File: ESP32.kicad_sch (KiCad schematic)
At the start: 39 parts, among them J4 JTAG, Q1 MMBT3904, Q2 MMBT3904, Q3 MMBT3904, Q4 MMBT3904, U1 ESP-WROVER-32, U3 CH340G, Y1 12M

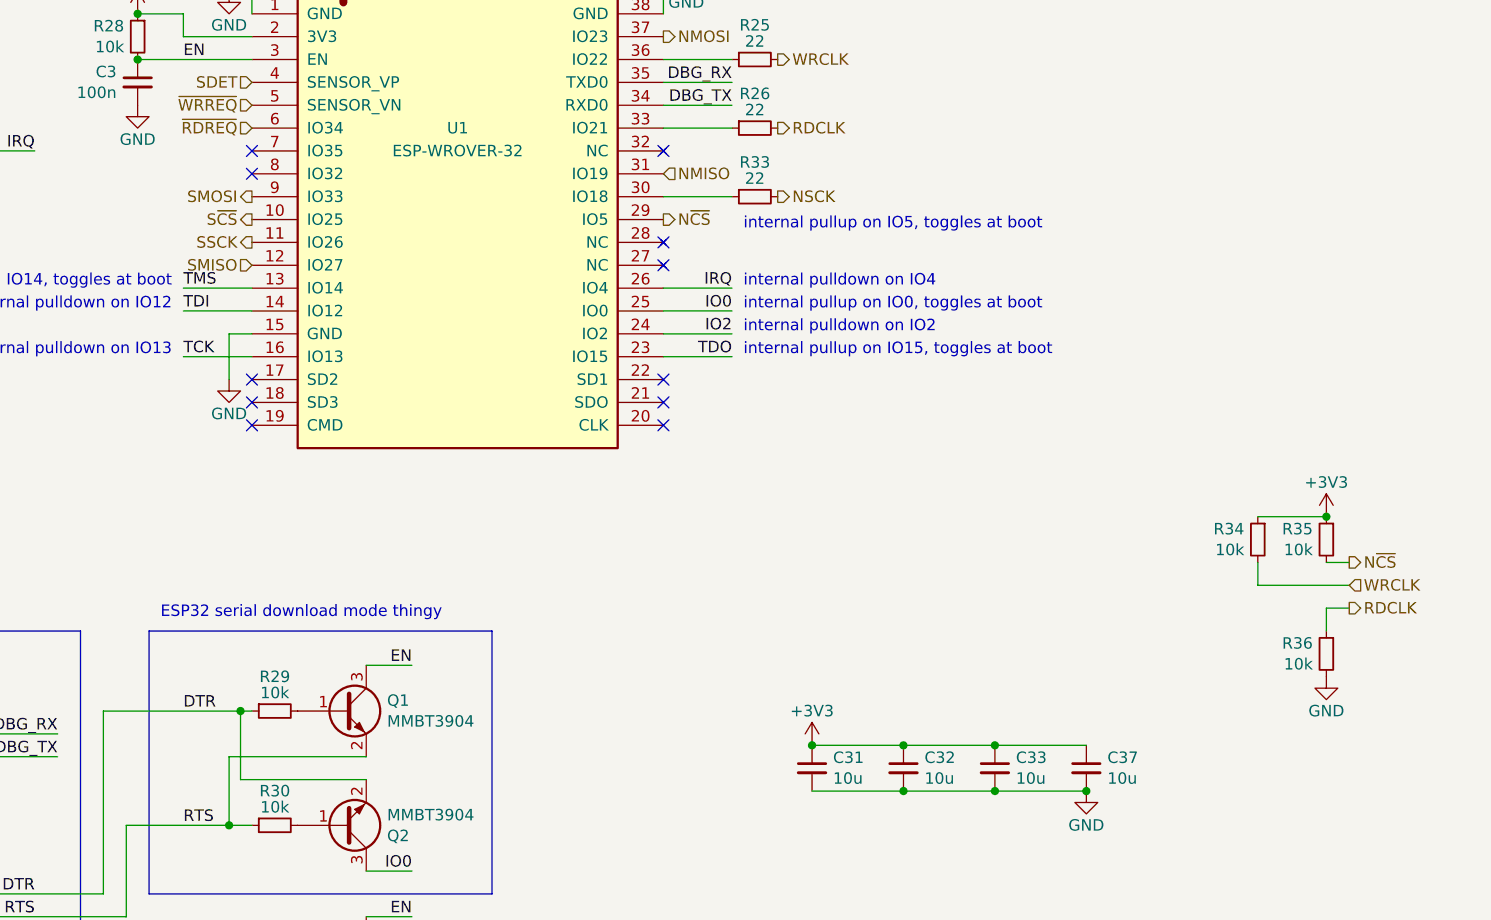
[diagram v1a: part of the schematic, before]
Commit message: Prototype with 74xx
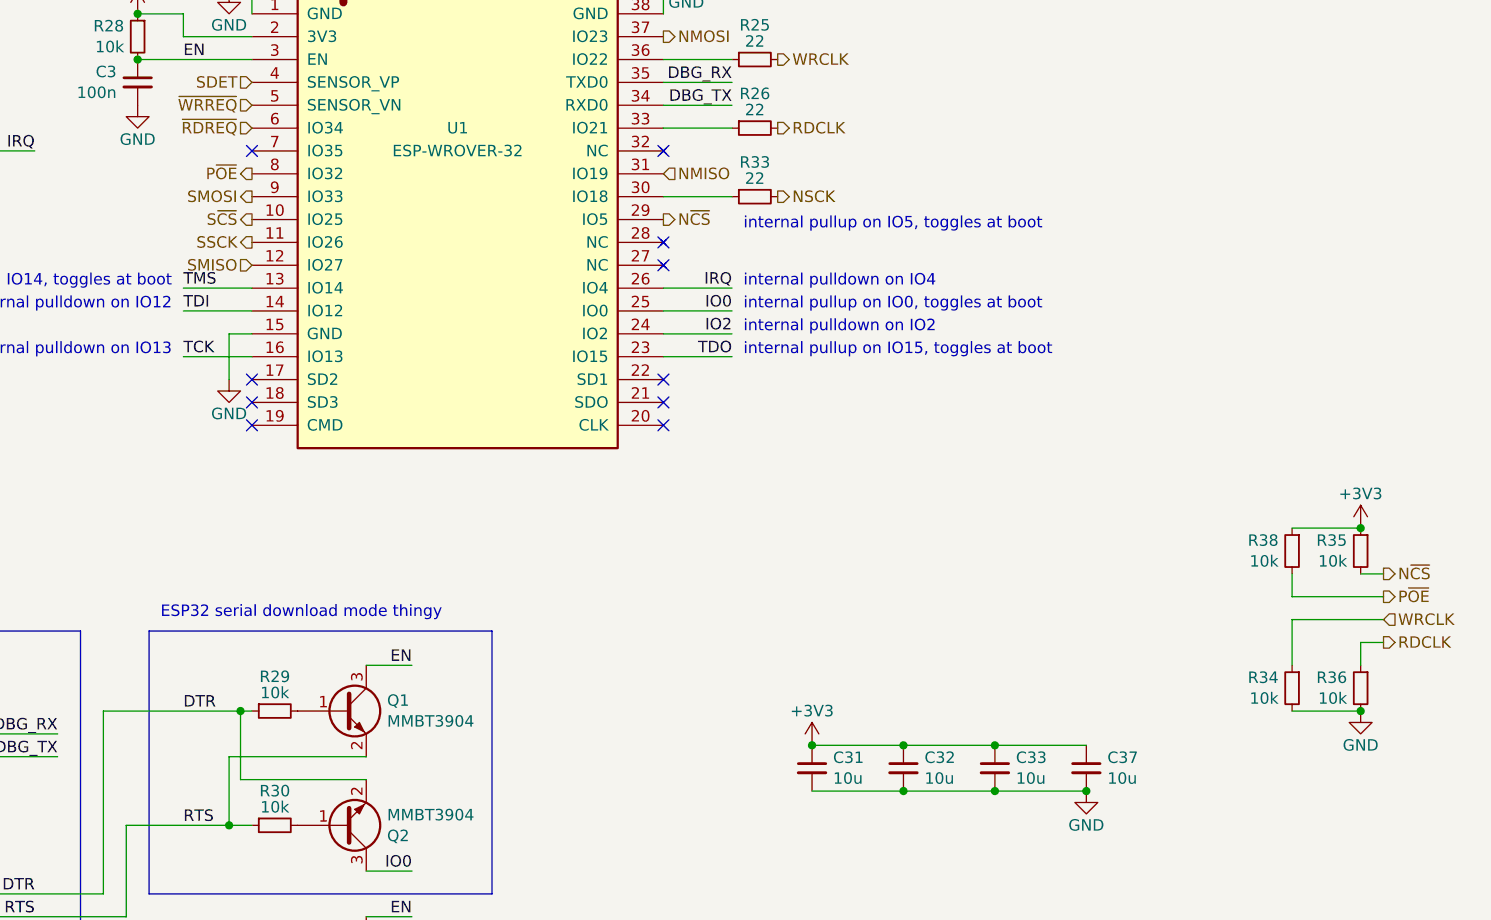
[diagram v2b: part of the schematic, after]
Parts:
- added R38: 10k, stdpads:R_0805, symbol Device:R_Small
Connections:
- net +3V3: now also R38.1; no longer R34.1
- net GND: now also R34.2
- net WRCLK: now also R34.1; no longer R34.2
- net P~{OE}: now reaches U1.8 (IO32)
- net P~{OE}: now also R38.2
- no-connect marks 17 -> 16
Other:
- moved on the sheet: R34, R35, R36
